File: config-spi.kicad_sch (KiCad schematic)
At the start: 38 parts, among them J1 0878311420, Q7 BSS138APW, Q8 BSS138APW, U1 XC7K70T-FBG484, U3 S25FL128SAGNFI000

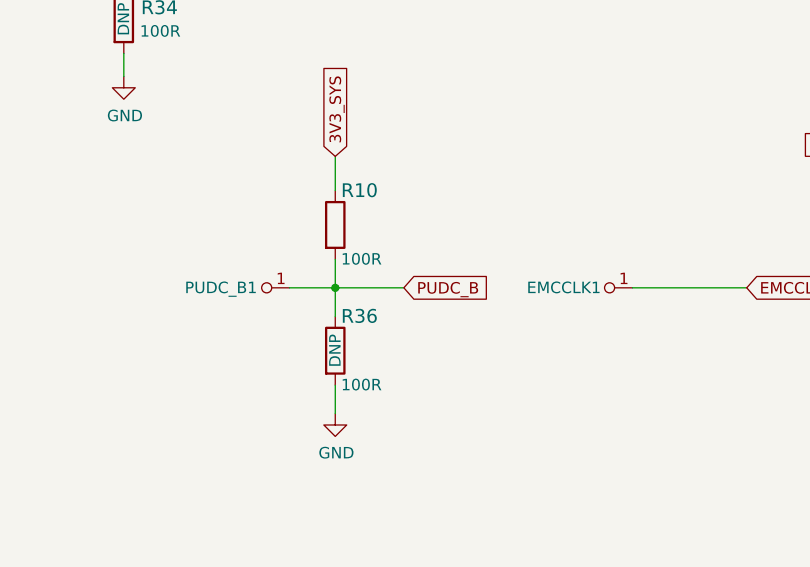
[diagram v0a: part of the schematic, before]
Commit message: Fix broken test-points
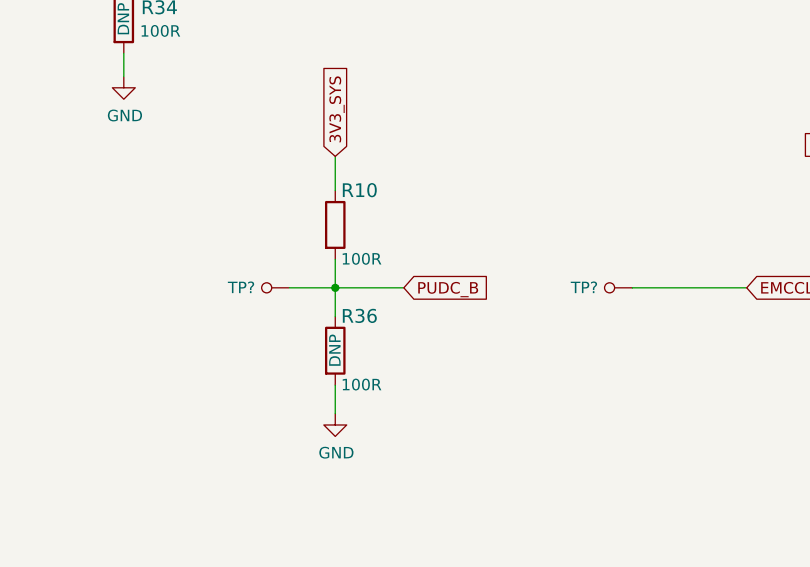
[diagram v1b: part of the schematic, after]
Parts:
- removed EMCCLK1, PUDC_B1: test, symbol lpddr4-test-board:test
- added TP? (x2): TP_SMD1MM, lpddr4-test-board-footprints:Testpoint_smd_1mm, symbol lpddr4-test-board:TP_SMD1MM
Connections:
- net EMCCLK: now also TP?.1
- net PUDC_B: now also TP?.1
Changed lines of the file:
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@@
     (pin "2")
-  )
-  (symbol (lib_id "lpddr4-test-board:test") (at 146.685 161.925 270) (unit 1)
-    (in_bom yes) (on_board yes)
-    (property "Reference" "PUDC_B1" (id 0) (at 144.145 160.655 90))
-    (property "Value" "test" (id 1) (at 150.4188 157.2514 90)
-      (effects (font (size 1.27 1.27)) hide)
-    )
-    (property "Footprint" "" (id 2) (at 146.685 161.925 0)
-      (effects (font (size 1.27 1.27)) hide)
-    )
-    (property "Datasheet" "" (id 3) (at 146.685 161.925 0)
-      (effects (font (size 1.27 1.27)) hide)
-    )
-    (pin "1")
-  )
-  (symbol (lib_id "lpddr4-test-board:test") (at 184.785 161.925 270) (unit 1)
-    (in_bom yes) (on_board yes)
-    (property "Reference" "EMCCLK1" (id 0) (at 182.245 160.655 90))
-    (property "Value" "test" (id 1) (at 188.5188 157.2514 90)
-      (effects (font (size 1.27 1.27)) hide)
-    )
-    (property "Footprint" "" (id 2) (at 184.785 161.925 0)
-      (effects (font (size 1.27 1.27)) hide)
-    )
-    (property "Datasheet" "" (id 3) (at 184.785 161.925 0)
-      (effects (font (size 1.27 1.27)) hide)
-    )
-    (pin "1")
   )
   (symbol (lib_id "lpddr4-test-board:R_100R_0402") (at 156.845 153.67 270) (unit 1)
@@
     )
     (pin "1")
+  )
+  (symbol (lib_id "lpddr4-test-board:TP_SMD1MM") (at 149.225 160.655 270) (unit 1)
+    (in_bom yes) (on_board yes)
+    (property "Reference" "TP?" (id 0) (at 147.955 160.655 90)
+      (effects (font (size 1.27 1.27)) (justify right))
+    )
+    (property "Value" "TP_SMD1MM" (id 1) (at 146.685 160.655 0)
+      (effects (font (size 1.27 1.27)) hide)
+    )
+    (property "Footprint" "lpddr4-test-board-footprints:Testpoint_smd_1mm" (id 2) (at 154.305 165.735 0)
+      (effects (font (size 1.524 1.524)) (justify left) hide)
+    )
+    (property "Datasheet" "" (id 3) (at 156.845 165.735 0)
+      (effects (font (size 1.524 1.524)) (justify left) hide)
+    )
+    (pin "1")
+  )
+  (symbol (lib_id "lpddr4-test-board:TP_SMD1MM") (at 187.325 160.655 270) (unit 1)
+    (in_bom yes) (on_board yes)
+    (property "Reference" "TP?" (id 0) (at 186.055 160.655 90)
+      (effects (font (size 1.27 1.27)) (justify right))
+    )
+    (property "Value" "TP_SMD1MM" (id 1) (at 184.785 160.655 0)
+      (effects (font (size 1.27 1.27)) hide)
+    )
+    (property "Footprint" "lpddr4-test-board-footprints:Testpoint_smd_1mm" (id 2) (at 192.405 165.735 0)
+      (effects (font (size 1.524 1.524)) (justify left) hide)
+    )
+    (property "Datasheet" "" (id 3) (at 194.945 165.735 0)
+      (effects (font (size 1.524 1.524)) (justify left) hide)
+    )
+    (pin "1")

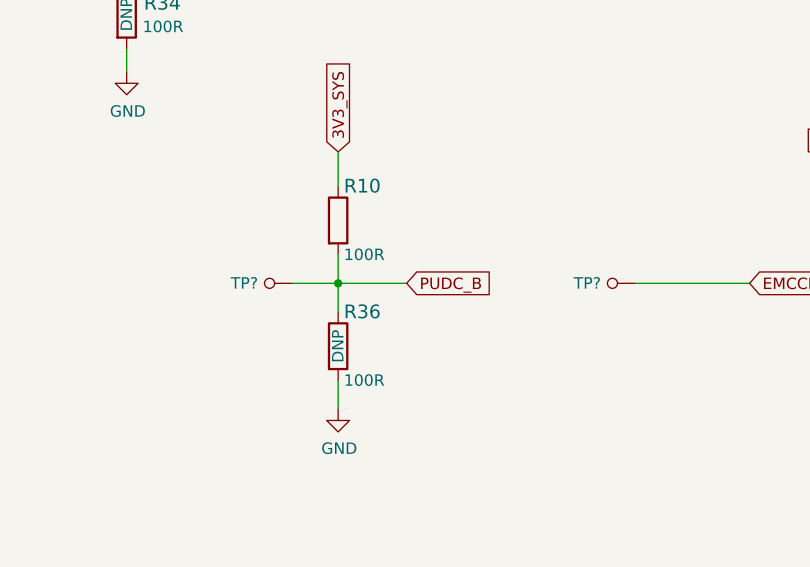
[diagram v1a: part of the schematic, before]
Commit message: Update power supplies to AP62600
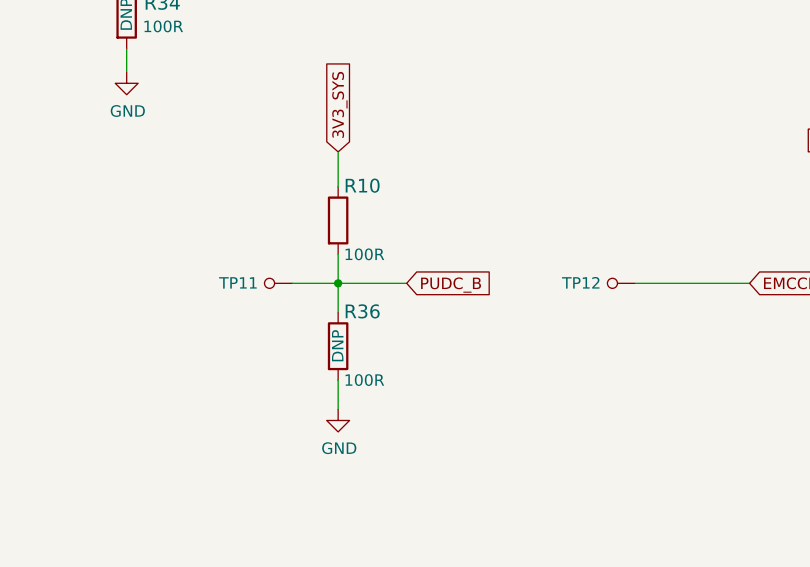
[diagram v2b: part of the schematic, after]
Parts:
- gave numbers to parts that had none: 2
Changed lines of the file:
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@@
   (symbol (lib_id "lpddr4-test-board:TP_SMD1MM") (at 149.225 160.655 270) (unit 1)
     (in_bom yes) (on_board yes)
-    (property "Reference" "TP?" (id 0) (at 147.955 160.655 90)
+    (property "Reference" "TP11" (id 0) (at 147.955 160.655 90)
       (effects (font (size 1.27 1.27)) (justify right))
     )
@@
   (symbol (lib_id "lpddr4-test-board:TP_SMD1MM") (at 187.325 160.655 270) (unit 1)
     (in_bom yes) (on_board yes)
-    (property "Reference" "TP?" (id 0) (at 186.055 160.655 90)
+    (property "Reference" "TP12" (id 0) (at 186.055 160.655 90)
       (effects (font (size 1.27 1.27)) (justify right))
     )

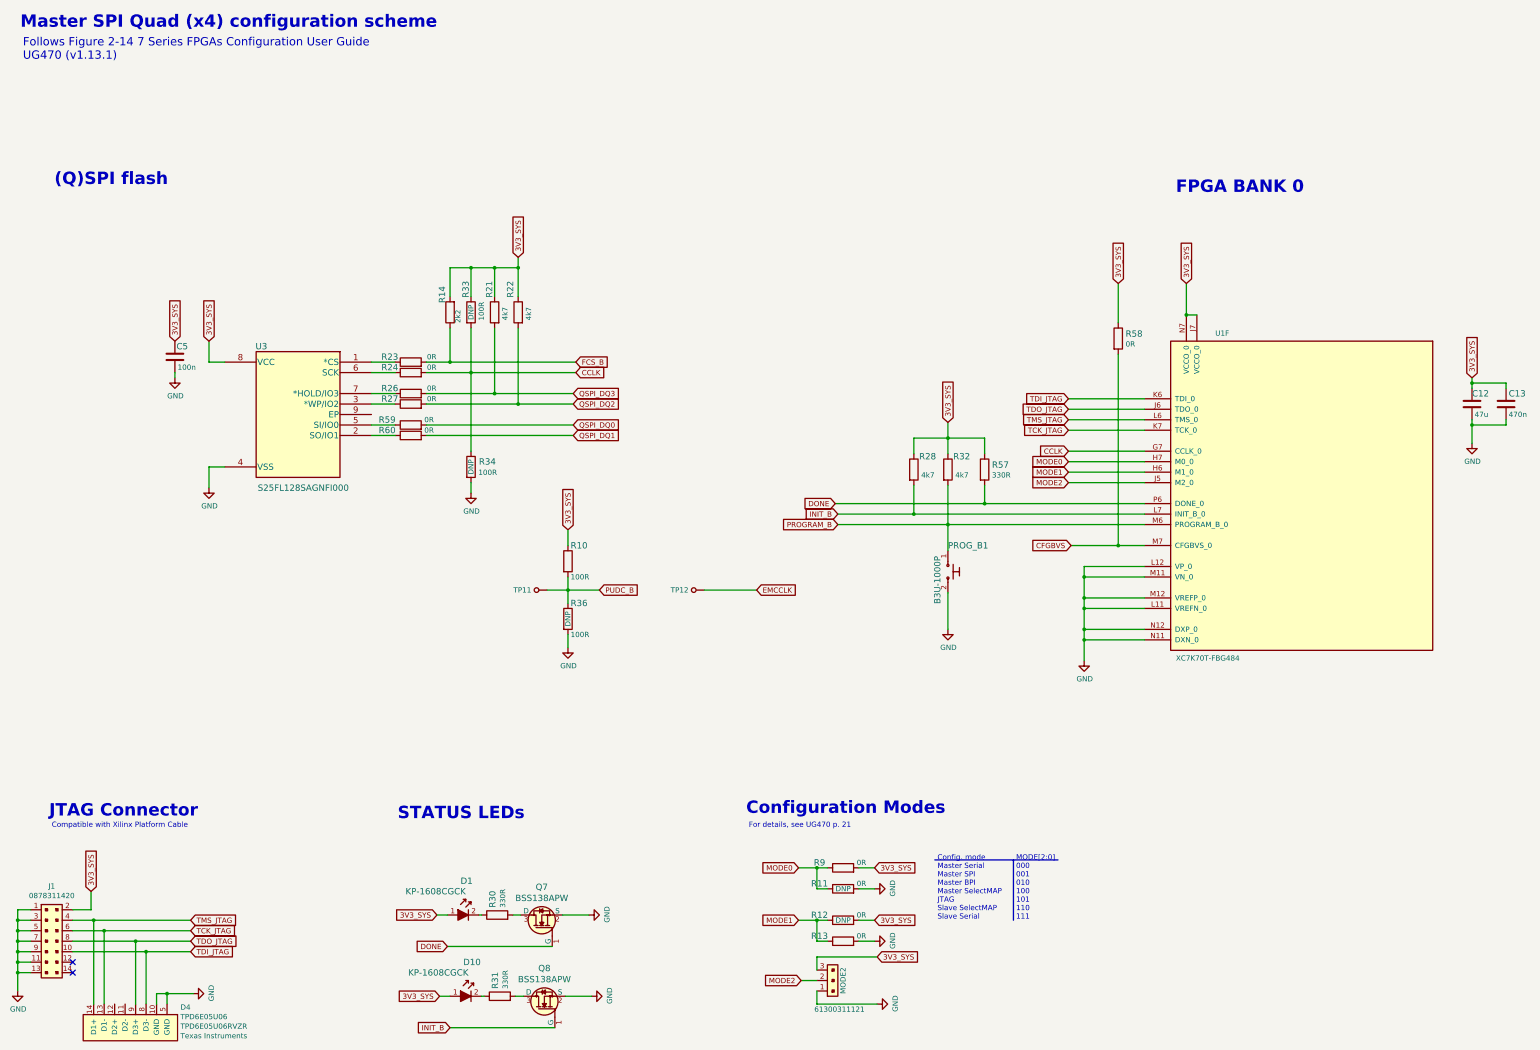
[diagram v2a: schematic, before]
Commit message: Placement and routing of FT4232H. Re annotation of the schematics
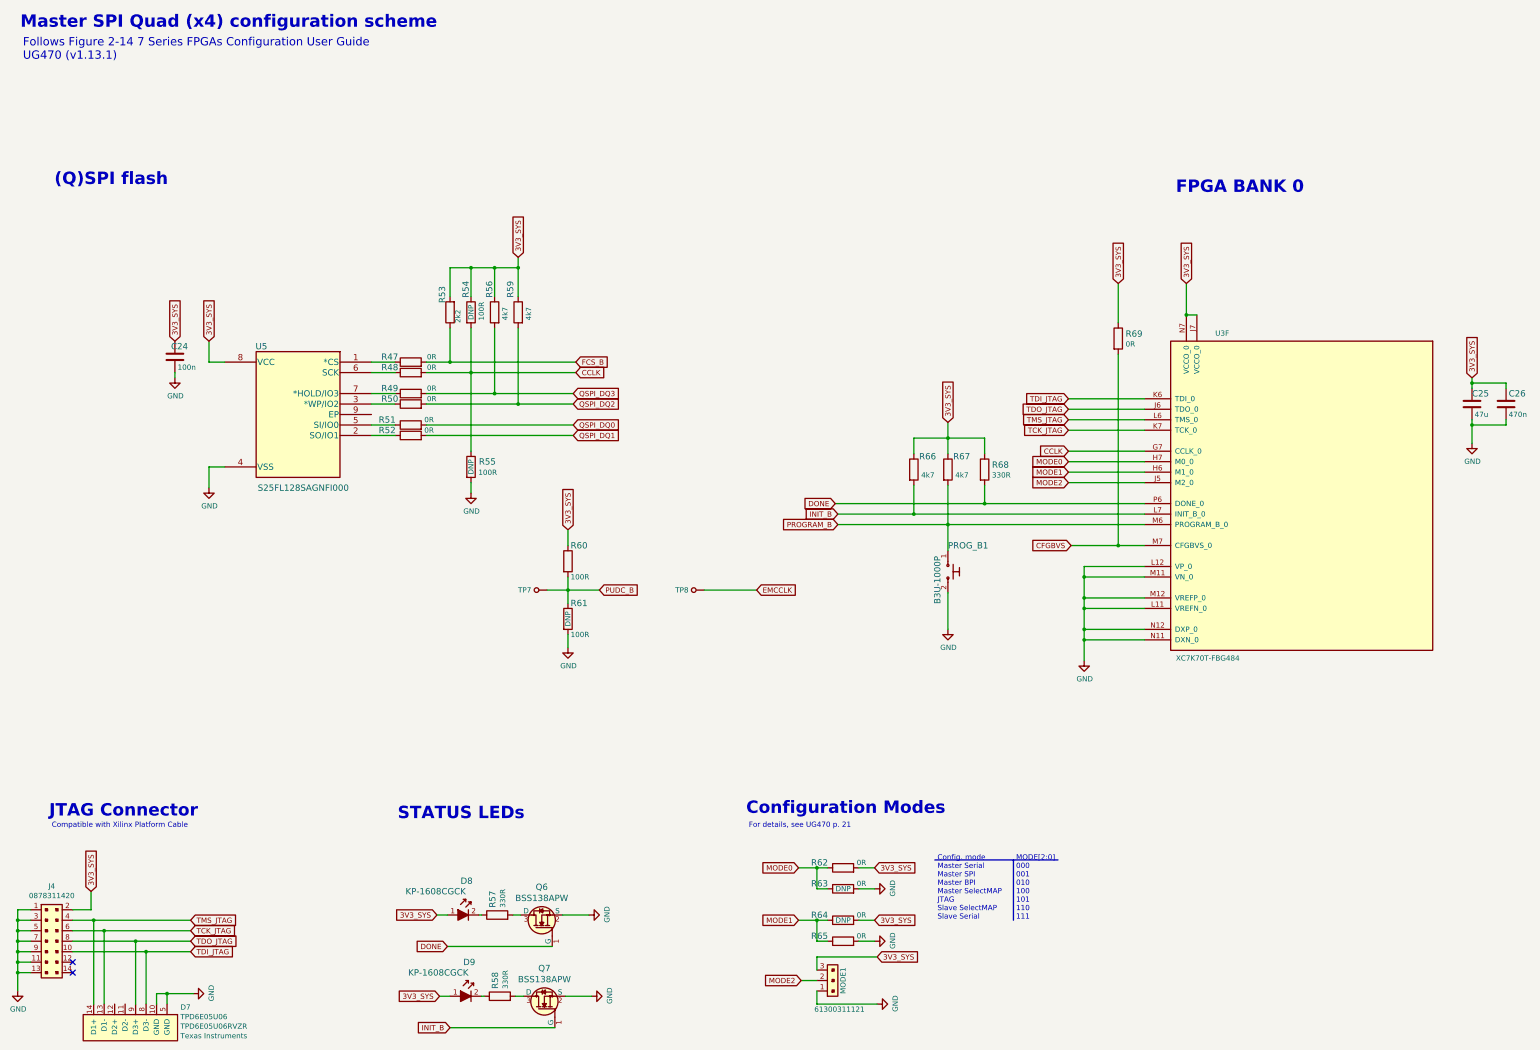
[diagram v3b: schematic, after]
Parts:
- renumbered C5 to C24, C12 to C25, C13 to C26, D4 to D7, D1 to D8, D10 to D9, J1 to J4, MODE2 to MODE1, Q7 to Q6, Q8 to Q7, R23 to R47, R24 to R48, R26 to R49, R27 to R50, R59 to R51, R60 to R52, R14 to R53, R33 to R54, R34 to R55, R21 to R56, R30 to R57, R31 to R58, R22 to R59, R10 to R60, R36 to R61, R9 to R62, R11 to R63, R12 to R64, R13 to R65, R28 to R66, R32 to R67, R57 to R68, R58 to R69, TP11 to TP7, TP12 to TP8, U1 to U3, U3 to U5
